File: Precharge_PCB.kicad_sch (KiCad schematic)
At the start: 72 parts, among them J1 MolexMicrofitPlus, J10 Conn_01x06, J2 MolexMicrofitPlus, J3 Conn_01x08, J4 MolexMicrofitPlus, J5 MolexMicrofitPlus, J6 MolexMicrofitPlus, K1 G2RL-1A, K2 G2RL-1A, Q1 DMN61D8LQ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

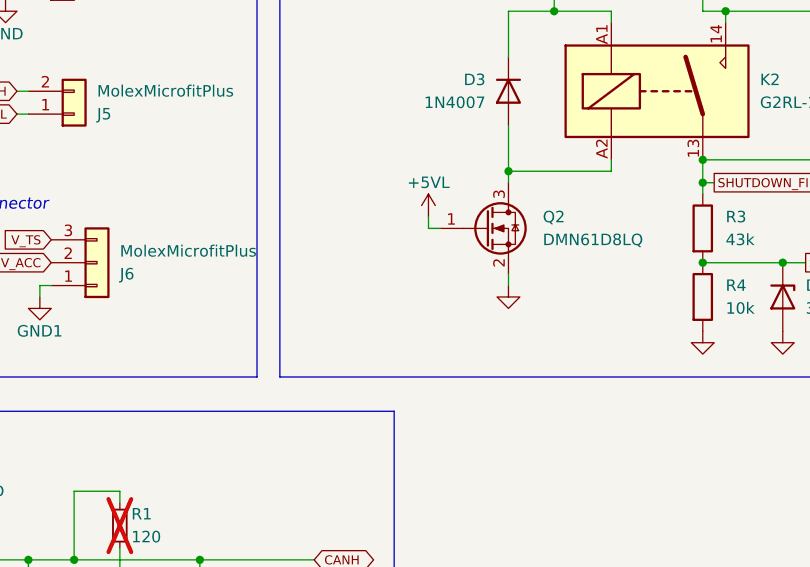
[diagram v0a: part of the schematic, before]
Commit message: schematic: Add a pull-down to the TSAL power detection MOSFET
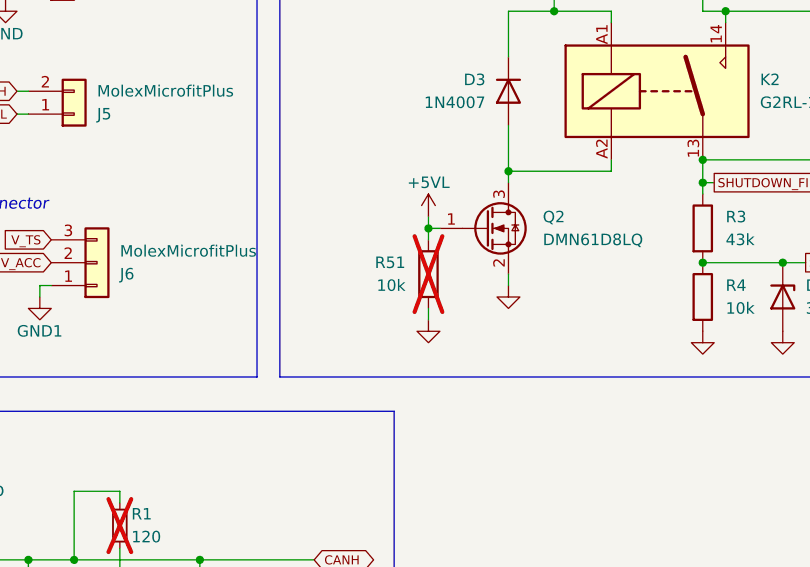
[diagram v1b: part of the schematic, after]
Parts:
- added R51: 10k, Resistor_SMD:R_0603_1608Metric, symbol Device:R
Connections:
- net +5VL: now also R51.1
- net GND: now also R51.2
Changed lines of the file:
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@@
 		(color 0 0 0 0)
 	)
+	(junction
+		(at 107.95 134.62)
+		(diameter 0)
+		(color 0 0 0 0)
+	)
 	(no_connect
 		(at 243.84 137.16)
@@
 	(wire
 		(pts
+			(xy 107.95 134.62) (xy 107.95 135.89)
+		)
+		(stroke
+			(width 0)
+			(type default)
+		)
+	)
+	(wire
+		(pts
 			(xy 64.77 142.24) (xy 64.77 140.97)
 		)
@@
 	(wire
 		(pts
+			(xy 107.95 143.51) (xy 107.95 144.78)
+		)
+		(stroke
+			(width 0)
+			(type default)
+		)
+	)
+	(wire
+		(pts
 			(xy 181.61 71.12) (xy 181.61 72.39)
 		)
@@
 	)
 	(symbol
+		(lib_id "Device:R")
+		(at 107.95 139.7 0)
+		(mirror y)
+		(unit 1)
+		(exclude_from_sim no)
+		(in_bom yes)
+		(on_board yes)
+		(dnp yes)
+		(fields_autoplaced yes)
+		(property "Reference" "R51"
+			(at 105.41 138.4299 0)
+			(effects
+				(font
+					(size 1.27 1.27)
+				)
+				(justify left)
+			)
+		)
+		(property "Value" "10k"
+			(at 105.41 140.9699 0)
+			(effects
+				(font
+					(size 1.27 1.27)
+				)
+				(justify left)
+			)
+		)
+		(property "Footprint" "Resistor_SMD:R_0603_1608Metric"
+			(at 109.728 139.7 90)
+			(effects
+				(font
+					(size 1.27 1.27)
+				)
+				(hide yes)
+			)
+		)
+		(property "Datasheet" "~"
+			(at 107.95 139.7 0)
+			(effects
+				(font
+					(size 1.27 1.27)
+				)
+				(hide yes)
+			)
+		)
+		(property "Description" "Resistor"
+			(at 107.95 139.7 0)
+			(effects
+				(font
+					(size 1.27 1.27)
+				)
+				(hide yes)
+			)
+		)
+		(pin "1"
+		)
+		(pin "2"
+		)
+		(instances
+			(project "Precharge_PCB"
+				(path "/c467677d-b98c-4488-bd11-965ef67263b2"
+					(reference "R51")
+					(unit 1)
+				)
+			)
+		)
+	)
+	(symbol
 		(lib_id "Connector_Generic:Conn_01x02")
 		(at 34.29 121.92 0)
@@
 					(unit 1)
 				)
+			)
+		)
+	)
+	(symbol
+		(lib_id "power:GND")
+		(at 107.95 144.78 0)
+		(mirror y)
+		(unit 1)
+		(exclude_from_sim no)
+		(in_bom yes)
+		(on_board yes)
+		(dnp no)
+		(fields_autoplaced yes)
+		(property "Reference" "#PWR093"
+			(at 107.95 151.13 0)
+			(effects
+				(font
+					(size 1.27 1.27)
+				)
+				(hide yes)
+			)
+		)
+		(property "Value" "GND"
+			(at 107.95 149.86 0)
+			(effects
+				(font
+					(size 1.27 1.27)
+				)
+				(hide yes)
+			)
+		)
+		(property "Footprint" ""
+			(at 107.95 144.78 0)
+			(effects
+				(font
+					(size 1.27 1.27)
+				)
+				(hide yes)
+			)
+		)
+		(property "Datasheet" ""
+			(at 107.95 144.78 0)
+			(effects
+				(font
+					(size 1.27 1.27)
+				)
+				(hide yes)
+			)
+		)
+		(property "Description" "Power symbol creates a global label with name \"GND\" , ground"
+			(at 107.95 144.78 0)
+			(effects
+				(font
+					(size 1.27 1.27)
+				)
+				(hide yes)
+			)
+		)
+		(pin "1"
+		)
+		(instances
+			(project "Precharge_PCB"
+				(path "/c467677d-b98c-4488-bd11-965ef67263b2"
+					(reference "#PWR093")
+					(unit 1)
+				)

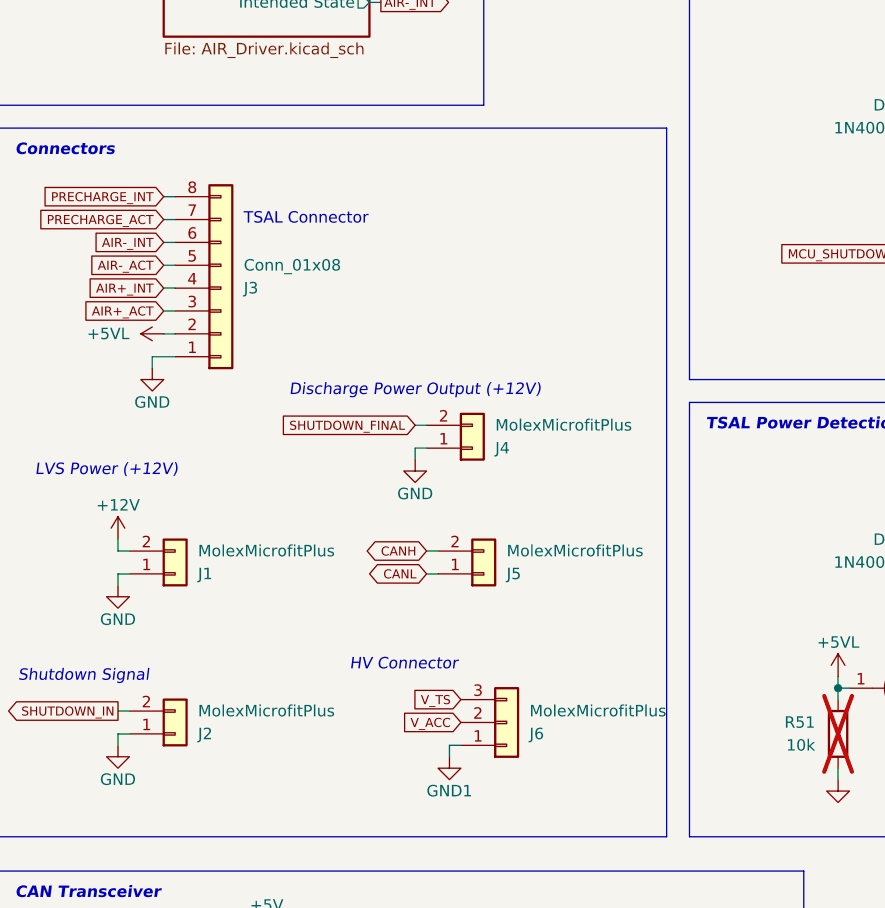
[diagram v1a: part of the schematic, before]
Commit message: schematic: Update molex connectors
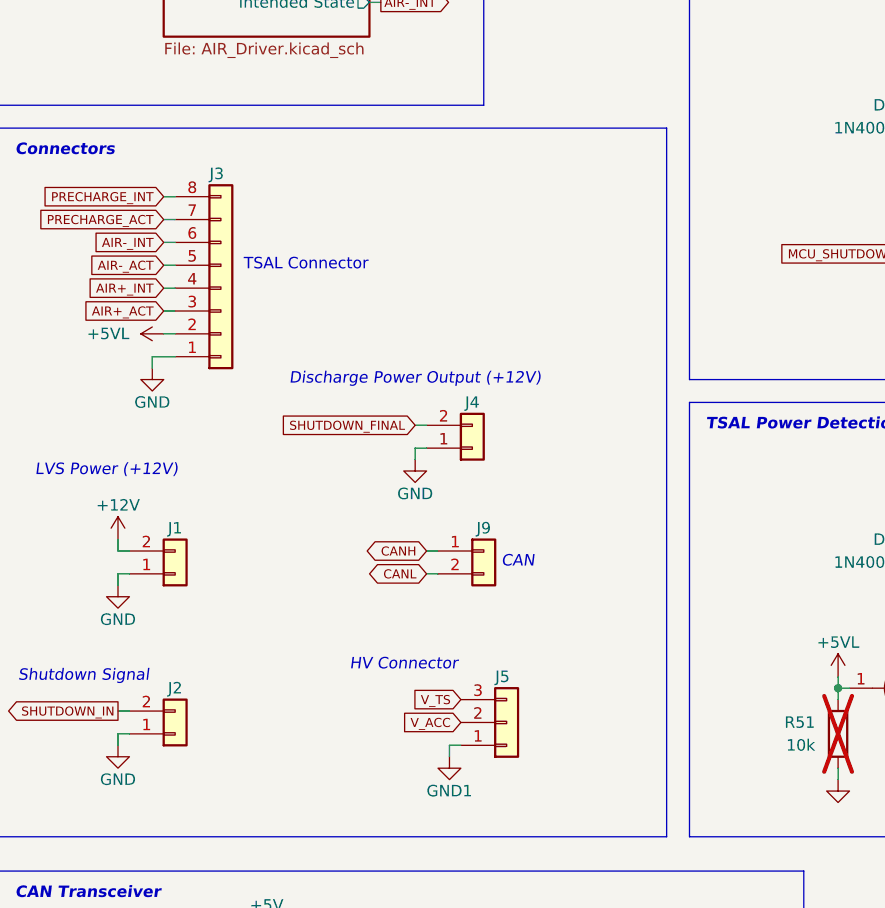
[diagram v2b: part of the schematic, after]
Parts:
- removed J5: MolexMicrofitPlus, MyLibrary:MolexMicrofitPlus1x2, symbol Connector_Generic:Conn_01x02
- removed J6: MolexMicrofitPlus, MyLibrary:MolexMicrofitPlus1x3, symbol Connector_Generic:Conn_01x03
- added J5: Conn_01x03, yfs:MolexMicrofitPlus1x3, symbol Connector_Generic:Conn_01x03
- added J9: Conn_01x02, yfs:MolexMicrofitPlus1x2, symbol Connector_Generic:Conn_01x02
- J1: value MolexMicrofitPlus -> Conn_01x02; footprint MyLibrary:MolexMicrofitPlus1x2 -> yfs:MolexMicrofitPlus1x2; Dist (none) -> Mouser; Dist # (none) -> 538-215760-1022; Mfr (none) -> Molex; Mfr # (none) -> 2157601022
- J2: value MolexMicrofitPlus -> Conn_01x02; footprint MyLibrary:MolexMicrofitPlus1x2 -> yfs:MolexMicrofitPlus1x2; Dist (none) -> Mouser; Dist # (none) -> 538-215760-1032; Mfr (none) -> Molex; Mfr # (none) -> 2157601032
- J3: Dist (none) -> Mouser; Dist # (none) -> 538-215760-1008; Mfr (none) -> Molex; Mfr # (none) -> 2157601008
- J4: value MolexMicrofitPlus -> Conn_01x02; footprint MyLibrary:MolexMicrofitPlus1x2 -> yfs:MolexMicrofitPlus1x2; Dist (none) -> Mouser; Dist # (none) -> 538-215760-1002; Mfr (none) -> Molex; Mfr # (none) -> 2157601002
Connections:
- net CANH: now also J9.1 (Pin_1)
- net CANL: now also J9.2 (Pin_2)
- net GND1: now also J5.1 (Pin_1)
- net V_ACC: now also J5.2 (Pin_2)
- net V_TS: now also J5.3 (Pin_3)
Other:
- note added: "CAN"

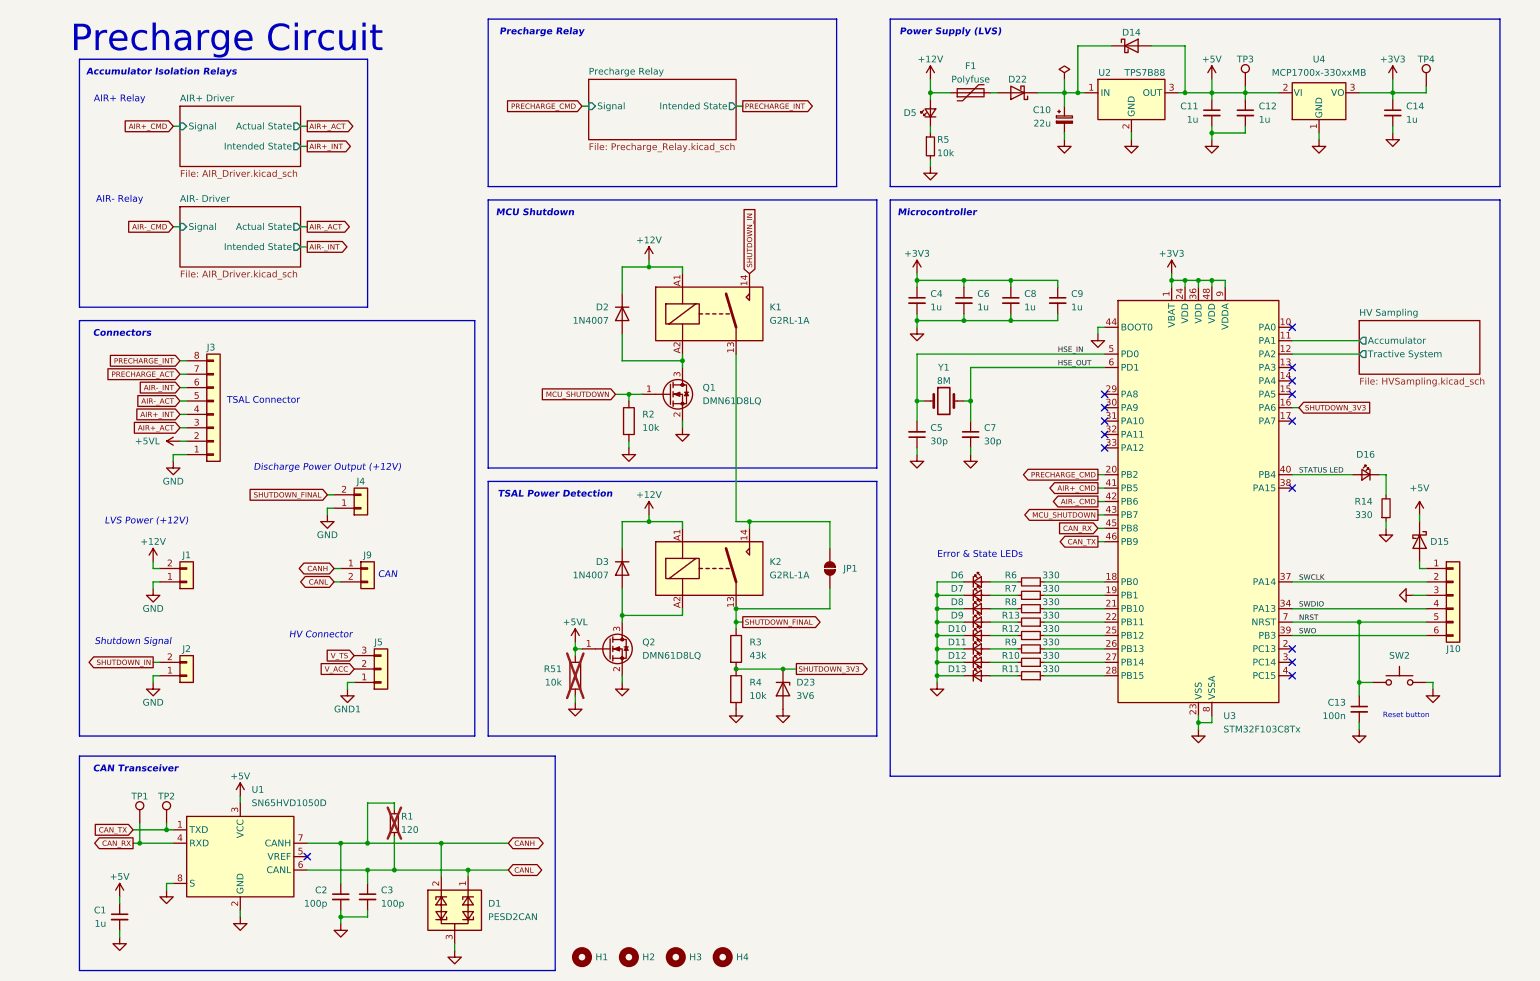
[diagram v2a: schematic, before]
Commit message: *: Use kicad-library exclusively
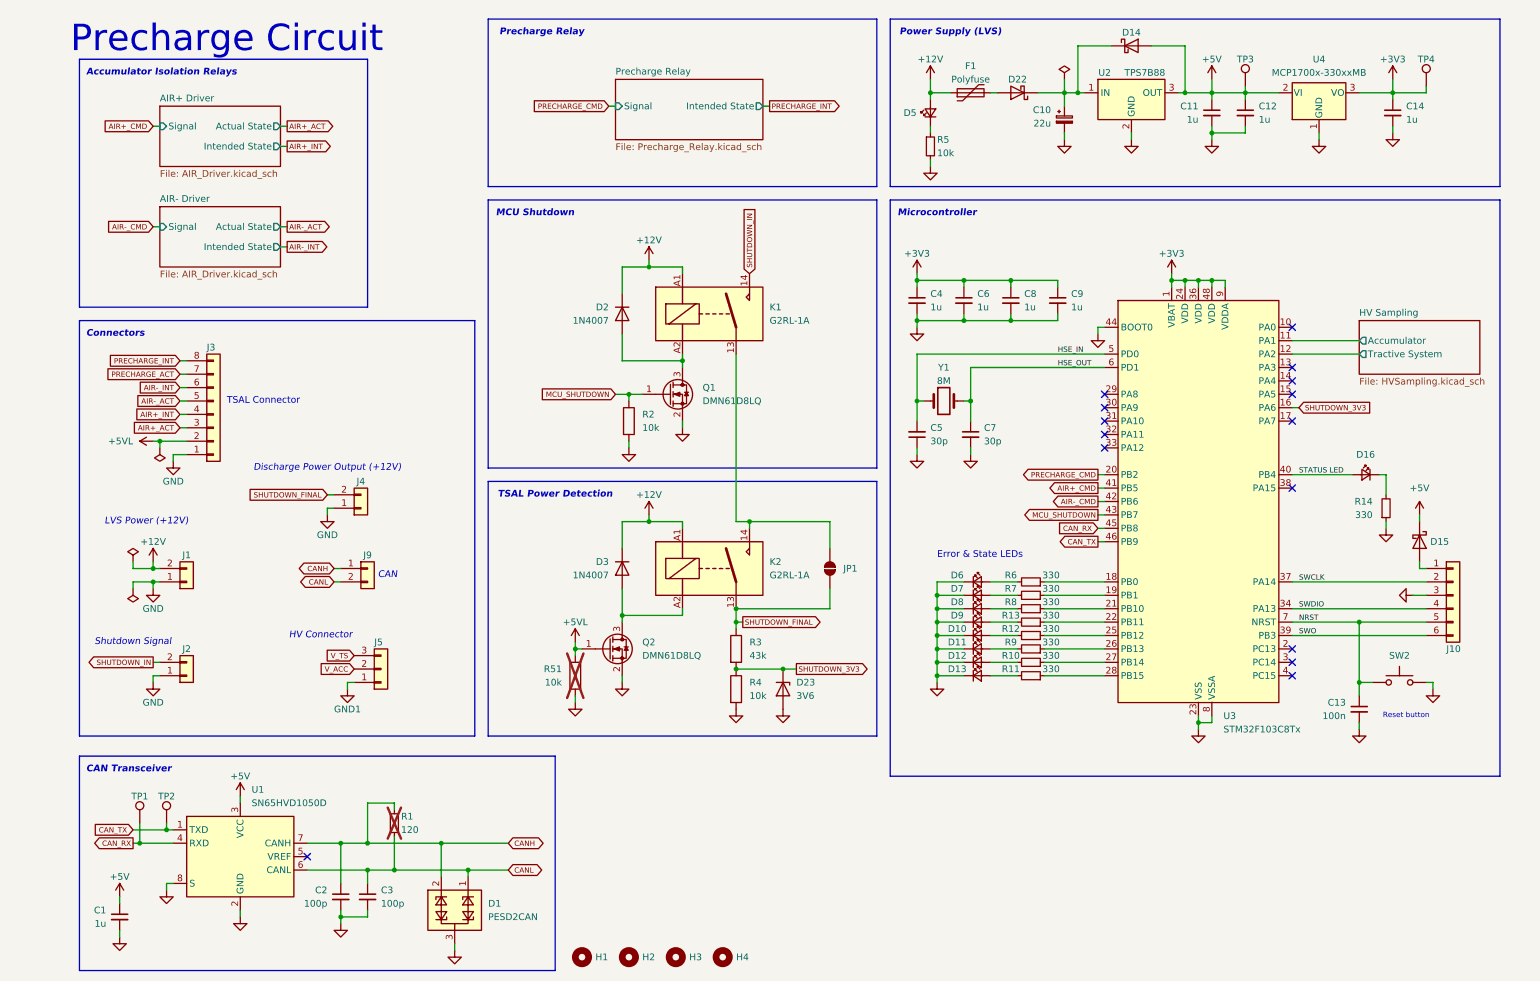
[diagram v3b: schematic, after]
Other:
- note removed: "AIR+ Relay"
- note removed: "AIR- Relay"

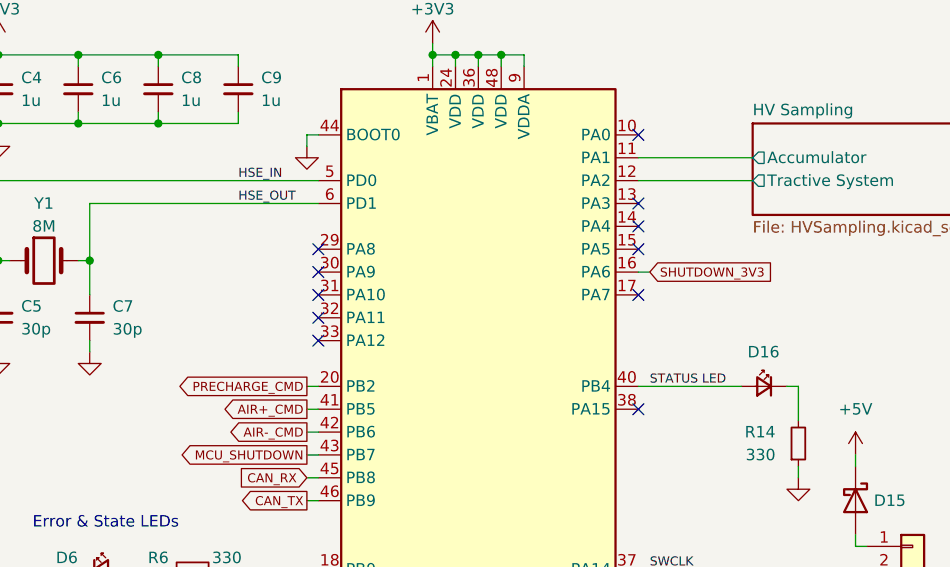
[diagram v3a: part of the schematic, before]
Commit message: schematic: Connect relay actual states to the MCU
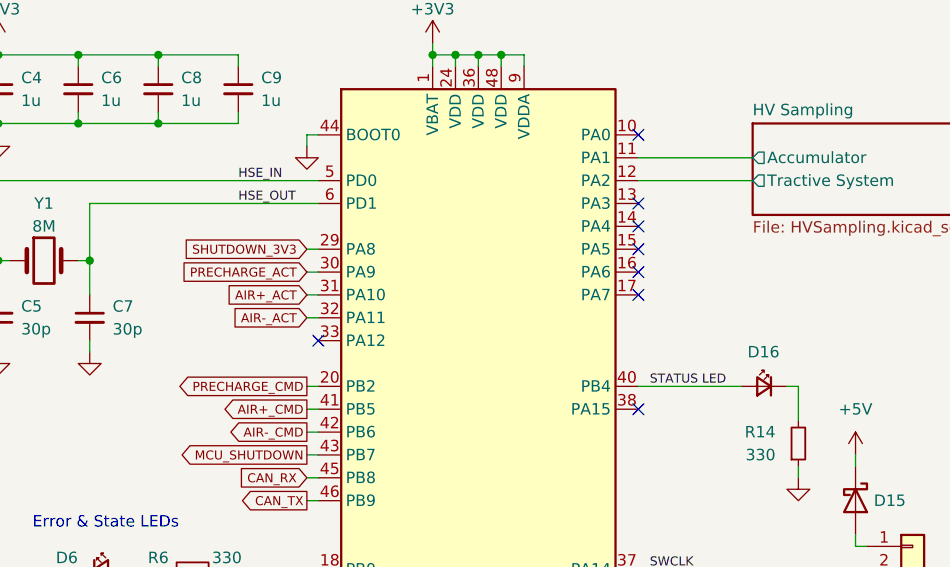
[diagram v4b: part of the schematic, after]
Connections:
- net AIR+_ACT: now also U3.31 (PA10)
- net AIR-_ACT: now also U3.32 (PA11)
- net PRECHARGE_ACT: now also U3.30 (PA9)
- net SHUTDOWN_3V3: now also U3.29 (PA8); no longer U3.16 (PA6)
- no-connect marks 15 -> 12
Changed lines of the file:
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@@
 	)
 	(no_connect
-		(at 208.28 93.98)
-	)
-	(no_connect
-		(at 208.28 88.9)
-	)
-	(no_connect
 		(at 243.84 104.14)
 	)
@@
 	)
 	(no_connect
-		(at 208.28 86.36)
-	)
-	(no_connect
 		(at 243.84 73.66)
 	)
@@
 	)
 	(no_connect
+		(at 243.84 88.9)
+	)
+	(no_connect
 		(at 243.84 139.7)
 	)
@@
 		(at 243.84 86.36)
 	)
-	(no_connect
-		(at 208.28 91.44)
-	)
 	(wire
 		(pts
@@
 	(wire
 		(pts
+			(xy 207.01 93.98) (xy 208.28 93.98)
+		)
+		(stroke
+			(width 0)
+			(type default)
+		)
+	)
+	(wire
+		(pts
 			(xy 223.52 66.04) (xy 223.52 64.77)
 		)
@@
 	(wire
 		(pts
+			(xy 207.01 91.44) (xy 208.28 91.44)
+		)
+		(stroke
+			(width 0)
+			(type default)
+		)
+	)
+	(wire
+		(pts
 			(xy 228.6 36.83) (xy 228.6 35.56)
 		)
@@
 	(wire
 		(pts
+			(xy 207.01 86.36) (xy 208.28 86.36)
+		)
+		(stroke
+			(width 0)
+			(type default)
+		)
+	)
+	(wire
+		(pts
 			(xy 243.84 129.54) (xy 256.54 129.54)
 		)
@@
 	(wire
 		(pts
+			(xy 207.01 88.9) (xy 208.28 88.9)
+		)
+		(stroke
+			(width 0)
+			(type default)
+		)
+	)
+	(wire
+		(pts
 			(xy 199.39 66.04) (xy 199.39 64.77)
 		)
@@
 	(wire
 		(pts
-			(xy 243.84 88.9) (xy 245.11 88.9)
-		)
-		(stroke
-			(width 0)
-			(type default)
-		)
-	)
-	(wire
-		(pts
 			(xy 116.84 128.27) (xy 116.84 129.54)
 		)
@@
 	(global_label "SHUTDOWN_3V3"
 		(shape input)
-		(at 245.11 88.9 0)
+		(at 207.01 86.36 180)
 		(fields_autoplaced yes)
 		(effects
@@
 				(size 1 1)
 			)
-			(justify left)
+			(justify right)
 		)
 		(property "Intersheetrefs" "${INTERSHEET_REFS}"
-			(at 259.0317 88.9 0)
+			(at 193.0883 86.36 0)
 			(effects
 				(font
 					(size 1.27 1.27)
 				)
-				(justify left)
+				(justify right)
 				(hide yes)
 			)
@@
 		)
 	)
+	(global_label "AIR+_ACT"
+		(shape input)
+		(at 207.01 91.44 180)
+		(fields_autoplaced yes)
+		(effects
+			(font
+				(size 1 1)
+			)
+			(justify right)
+		)
+		(property "Intersheetrefs" "${INTERSHEET_REFS}"
+			(at 197.7074 91.44 0)
+			(effects
+				(font
+					(size 1.27 1.27)
+				)
+				(justify right)
+				(hide yes)
+			)
+		)
+	)
+	(global_label "PRECHARGE_ACT"
+		(shape input)
+		(at 207.01 88.9 180)
+		(fields_autoplaced yes)
+		(effects
+			(font
+				(size 1 1)
+			)
+			(justify right)
+		)
+		(property "Intersheetrefs" "${INTERSHEET_REFS}"
+			(at 192.5645 88.9 0)
+			(effects
+				(font
+					(size 1.27 1.27)
+				)
+				(justify right)
+				(hide yes)
+			)
+		)
+	)
 	(global_label "AIR-_CMD"
 		(shape output)
@@
 			(effects
 				(font
+					(size 1.27 1.27)
+				)
+				(justify right)
+				(hide yes)
+			)
+		)
+	)
+	(global_label "AIR-_ACT"
+		(shape input)
+		(at 207.01 93.98 180)
+		(fields_autoplaced yes)
+		(effects
+			(font
+				(size 1 1)
+			)
+			(justify right)
+		)
+		(property "Intersheetrefs" "${INTERSHEET_REFS}"
+			(at 197.7074 93.98 0)
+			(effects
+				(font
